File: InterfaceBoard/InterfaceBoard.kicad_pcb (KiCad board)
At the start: 2 copper layers, 100 x 86 mm, 167 parts, among them J1 SWD, J2 USB_B, J3 Keithley_50-Pin_Connector, J4 DB9_Female_MountingHoles, J5 SPI, J6 RS232, J7 UART, P1 RB1-125BAG1A, Q1 BC848W, Q2 BC848W, Q3 BC848W, U1 W5500, U2 FT231XQ, U3 MAX3232, U4 STM32G0B1RET, U5 AP62250Z6, Y1 25 MHz, Y2 32.768 kHz, Y3 24 MHz

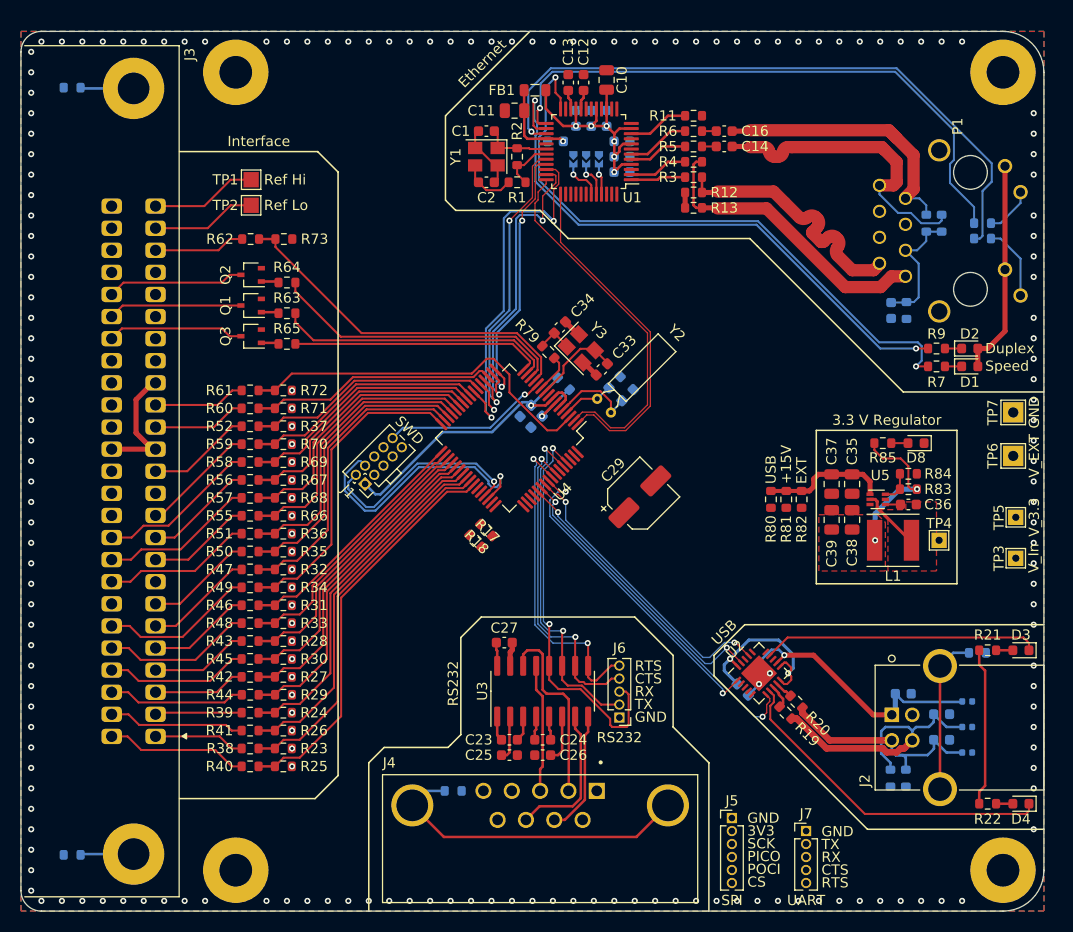
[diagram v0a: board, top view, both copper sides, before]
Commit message: InterfaceBoard: Place and route buttons and LEDs.
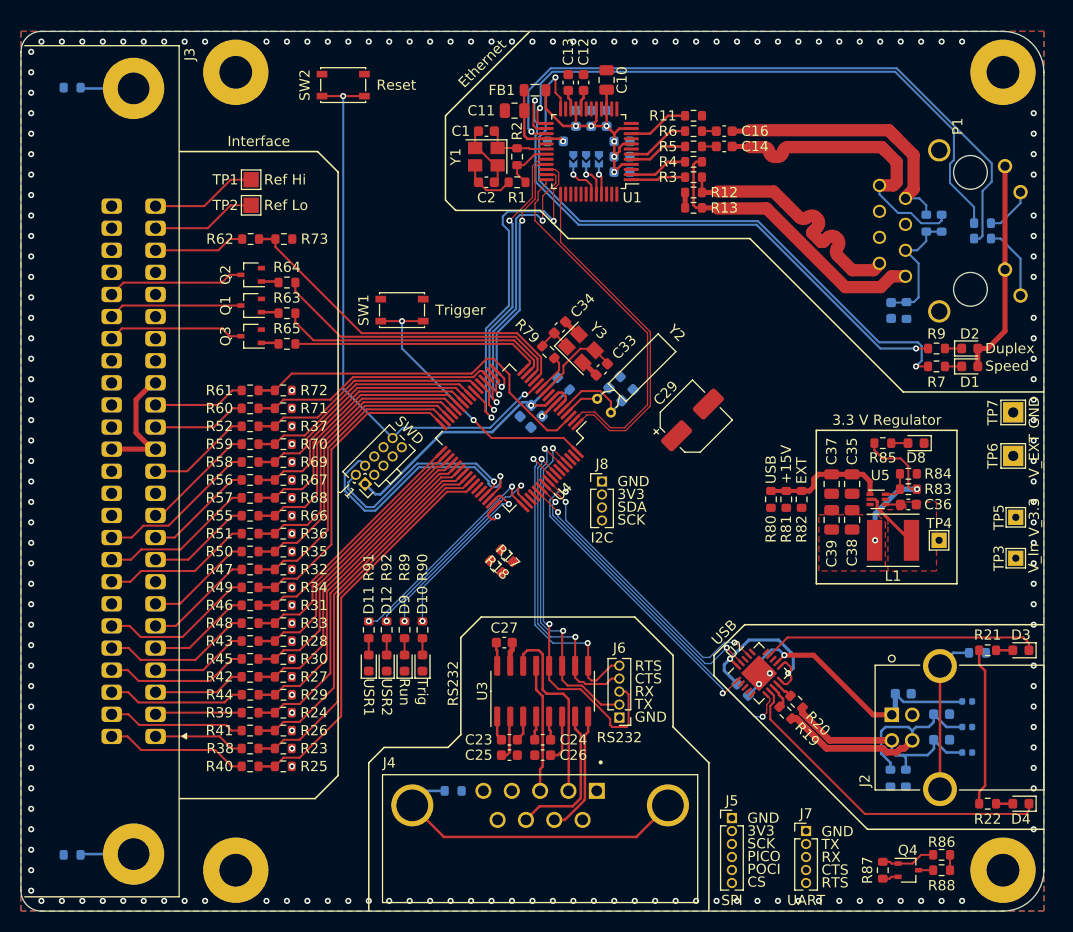
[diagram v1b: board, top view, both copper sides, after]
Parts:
- added D10: Red, LED_SMD:LED_0603_1608Metric, F.Cu at (79.2, 90.8)
- added D11: Red, LED_SMD:LED_0603_1608Metric, F.Cu at (74.0, 90.8)
- added D12: Red, LED_SMD:LED_0603_1608Metric, F.Cu at (75.7, 90.8)
- added D9: Red, LED_SMD:LED_0603_1608Metric, F.Cu at (77.5, 90.8)
- added J8: I2C, Connector_PinHeader_1.27mm:PinHeader_1x04_P1.27mm_Vertical, F.Cu at (96.8, 73.0)
- added Q4: BC856W, Package_TO_SOT_SMD:SOT-323_SC-70, F.Cu at (126.8, 111.0)
- added R86: 10k, Resistor_SMD:R_0603_1608Metric, F.Cu at (130.0, 109.5)
- added R87: 180k, Resistor_SMD:R_0603_1608Metric, F.Cu at (124.2, 111.0)
- added R88: 0, Resistor_SMD:R_0603_1608Metric, F.Cu at (130.0, 111.0)
- added R89: 1.8k, Resistor_SMD:R_0603_1608Metric, F.Cu at (77.5, 87.5)
- added R90: 1.8k, Resistor_SMD:R_0603_1608Metric, F.Cu at (79.2, 87.5)
- added R91: 1.8k, Resistor_SMD:R_0603_1608Metric, F.Cu at (74.0, 87.5)
- added R92: 1.8k, Resistor_SMD:R_0603_1608Metric, F.Cu at (75.7, 87.5)
- added SW1: PTS810, Button_Switch_SMD:SW_SPST_PTS810, F.Cu at (77.2, 56.2)
- added SW2: PTS810, Button_Switch_SMD:SW_SPST_PTS810, F.Cu at (71.5, 34.2)
- moved C29 9.11 mm to (105.6, 67.0)
- moved R17 3.20 mm to (87.5, 80.2)
- moved R18 3.20 mm to (86.4, 81.3)
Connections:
- R75 pad 2: /MCU/USB_PULLUP -> Net-(R75-Pad2)
- R76 pad 2: /MCU/USB_PULLUP -> Net-(R75-Pad2)
- U4 pad 47: unconnected-(U4-Pad47) -> /MCU/LED_RUN
- U4 pad 48: unconnected-(U4-Pad48) -> /MCU/LED_TRIG
- U4 pad 49: unconnected-(U4-Pad49) -> /MCU/LED_USR1
- U4 pad 50: unconnected-(U4-Pad50) -> /MCU/LED_USR2
- U4 pad 59: unconnected-(U4-Pad59) -> /MCU/USB_PULLUP
- U4 pad 64: unconnected-(U4-Pad64) -> /MCU/BTN_TRIG
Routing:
- net /MCU/NRST: track 16.4 -> 56.0 mm, vias 1 -> 2
- net /MCU/BTN_TRIG: track 0.00 -> 28.2 mm, vias 0 -> 2
- net /MCU/LED_USR1: track 0.00 -> 21.8 mm, vias 0 -> 2
- net /MCU/LED_USR2: track 0.00 -> 21.1 mm, vias 0 -> 2
- net /MCU/LED_RUN: track 0.00 -> 18.3 mm, vias 0 -> 2
- net /MCU/LED_TRIG: track 0.00 -> 15.9 mm, vias 0 -> 2
- net Net-(Q4-Pad1): track 0.00 -> 5.35 mm
- net Net-(D11-Pad2): track 0.00 -> 1.64 mm
- net Net-(D9-Pad2): track 0.00 -> 1.64 mm
- net Net-(D12-Pad2): track 0.00 -> 1.64 mm
- net Net-(D10-Pad2): track 0.00 -> 1.64 mm
- net +3V3: track 78.3 -> 79.9 mm
- net /MCU/USB_PULLUP: track 0.00 -> 1.50 mm
- net Net-(R75-Pad2): track 0.00 -> 1.43 mm
- net /Ethernet Interface/POCI: track 35.5 -> 36.2 mm
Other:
- board text added: "Reset"
- board text added: "Run"
- board text added: "SDA"
- board text added: "Trig"
- board text added: "Trigger"
- board text added: "USR1"
- board text added: "USR2"

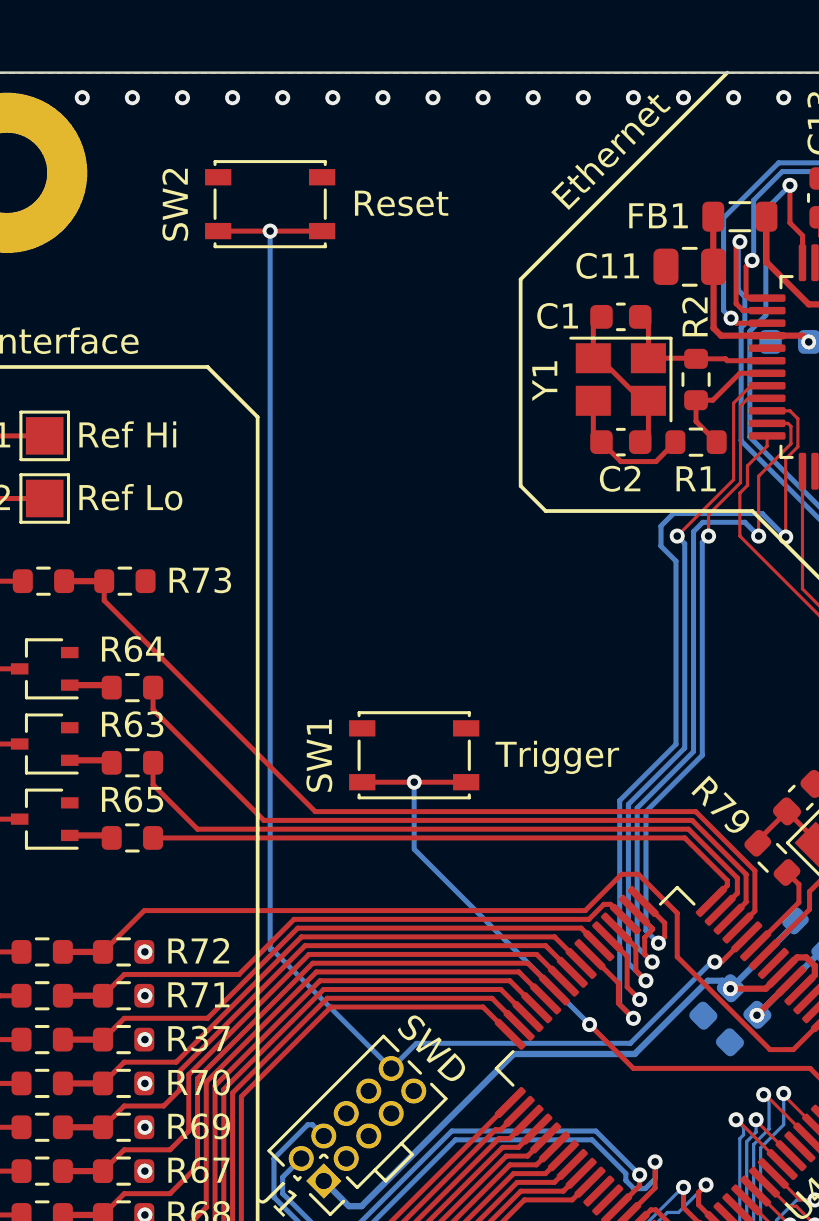
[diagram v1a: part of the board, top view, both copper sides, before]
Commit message: InterfaceBoard: Swap trigger and reset buttons
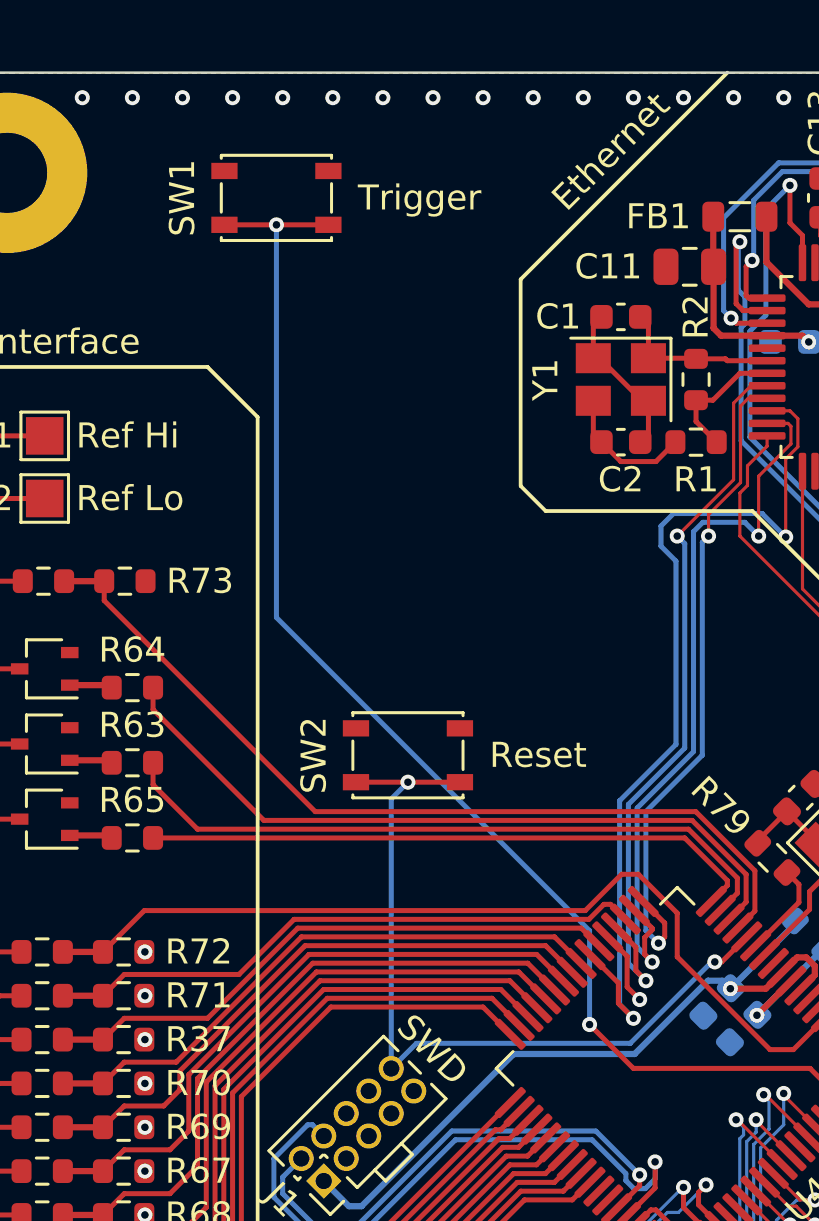
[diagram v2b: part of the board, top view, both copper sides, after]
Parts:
- moved SW1 22.9 mm to (71.8, 34.0)
- moved SW2 22.7 mm to (77.0, 56.2)
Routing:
- net /MCU/BTN_TRIG: track 28.2 -> 52.7 mm
- net /MCU/NRST: track 56.0 -> 32.2 mm
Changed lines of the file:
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@@
   )
   (footprint "Button_Switch_SMD:SW_SPST_PTS810" (layer "F.Cu")
-    (at 71.5 34.25)
+    (at 77 56.25)
     (descr "C&K Components, PTS 810 Series, Microminiature SMT Top Actuated, http://www.ckswitches.com/media/1476/pts810.pdf")
     (tags "SPST Button Switch")
@@
   )
   (footprint "Button_Switch_SMD:SW_SPST_PTS810" (layer "F.Cu")
-    (at 77.25 56.25)
+    (at 71.75 34)
     (descr "C&K Components, PTS 810 Series, Microminiature SMT Top Actuated, http://www.ckswitches.com/media/1476/pts810.pdf")
     (tags "SPST Button Switch")
@@
     (effects (font (size 1 1) (thickness 0.15)) (justify left))
   )
-  (gr_text "Trigger" (at 80.499999 56.25) (layer "F.SilkS")
+  (gr_text "Trigger" (at 74.999999 34) (layer "F.SilkS")
     (effects (font (size 1 1) (thickness 0.15)) (justify left))
   )
@@
     (effects (font (size 1 1) (thickness 0.15)) (justify left))
   )
-  (gr_text "Reset" (at 74.750001 34.249998) (layer "F.SilkS")
+  (gr_text "Reset" (at 80.250001 56.249998) (layer "F.SilkS")
     (effects (font (size 1 1) (thickness 0.15)) (justify left))
   )
@@
   (segment (start 89.525126 64.5) (end 90.525394 63.499732) (width 0.2) (layer "F.Cu") (net 16))
   (segment (start 89.25 64.5) (end 89.525126 64.5) (width 0.2) (layer "F.Cu") (net 16))
-  (segment (start 71.5 35.324999) (end 69.425 35.324999) (width 0.2) (layer "F.Cu") (net 16))
-  (segment (start 73.575 35.324999) (end 71.5 35.324999) (width 0.2) (layer "F.Cu") (net 16))
+  (segment (start 77 57.324999) (end 74.925 57.324999) (width 0.2) (layer "F.Cu") (net 16))
+  (segment (start 79.075 57.324999) (end 77 57.324999) (width 0.2) (layer "F.Cu") (net 16))
   (via (at 89.25 64.5) (size 0.6) (drill 0.3) (layers "F.Cu" "B.Cu") (free) (net 16))
-  (via (at 71.5 35.324999) (size 0.6) (drill 0.3) (layers "F.Cu" "B.Cu") (net 16))
+  (via (at 77 57.324999) (size 0.6) (drill 0.3) (layers "F.Cu" "B.Cu") (net 16))
   (segment (start 77.337833 67.75) (end 76.332897 68.754936) (width 0.2) (layer "B.Cu") (net 16))
-  (segment (start 71.577961 64) (end 76.332897 68.754936) (width 0.2) (layer "B.Cu") (net 16))
   (segment (start 85.875 67.75) (end 77.337833 67.75) (width 0.2) (layer "B.Cu") (net 16))
   (segment (start 89.25 64.5) (end 89.125 64.5) (width 0.2) (layer "B.Cu") (net 16))
+  (segment (start 76.332897 57.992102) (end 76.332897 68.754936) (width 0.2) (layer "B.Cu") (net 16))
   (segment (start 89.125 64.5) (end 85.875 67.75) (width 0.2) (layer "B.Cu") (net 16))
-  (segment (start 71.5 64) (end 71.577961 64) (width 0.2) (layer "B.Cu") (net 16))
-  (segment (start 71.5 35.324999) (end 71.5 64) (width 0.2) (layer "B.Cu") (net 16))
+  (segment (start 77 57.324999) (end 76.332897 57.992102) (width 0.2) (layer "B.Cu") (net 16))
   (segment (start 88.5 42.925) (end 89.325 43.75) (width 0.2) (layer "F.Cu") (net 20))
   (segment (start 89.175 42.075) (end 90.25 41) (width 0.2) (layer "F.Cu") (net 20))
@@
   (segment (start 87.8 74.5) (end 88.9 73.4) (width 0.127) (layer "B.Cu") (net 200))
   (segment (start 94.414481 70.111181) (end 93.0533 68.75) (width 0.2) (layer "F.Cu") (net 201))
-  (segment (start 77.25 57.325) (end 75.175 57.325) (width 0.2) (layer "F.Cu") (net 201))
+  (segment (start 71.75 35.075) (end 69.675 35.075) (width 0.2) (layer "F.Cu") (net 201))
   (segment (start 86 68.75) (end 84.25 67) (width 0.2) (layer "F.Cu") (net 201))
-  (segment (start 79.325001 57.325001) (end 77.25 57.325) (width 0.2) (layer "F.Cu") (net 201))
+  (segment (start 73.825001 35.075001) (end 71.75 35.075) (width 0.2) (layer "F.Cu") (net 201))
   (segment (start 93.0533 68.75) (end 86 68.75) (width 0.2) (layer "F.Cu") (net 201))
-  (via (at 77.25 57.325) (size 0.6) (drill 0.3) (layers "F.Cu" "B.Cu") (net 201))
+  (via (at 71.75 35.075) (size 0.6) (drill 0.3) (layers "F.Cu" "B.Cu") (net 201))
   (via (at 84.25 67) (size 0.6) (drill 0.3) (layers "F.Cu" "B.Cu") (net 201))
-  (segment (start 77.25 60) (end 77.25 57.325) (width 0.2) (layer "B.Cu") (net 201))
-  (segment (start 84.25 67) (end 77.25 60) (width 0.2) (layer "B.Cu") (net 201))
+  (segment (start 71.75 50.75) (end 84.25 63.25) (width 0.2) (layer "B.Cu") (net 201))
+  (segment (start 71.75 35.075) (end 71.75 50.75) (width 0.2) (layer "B.Cu") (net 201))
+  (segment (start 84.25 63.25) (end 84.25 67) (width 0.2) (layer "B.Cu") (net 201))
   (zone (net 4) (net_name "+3V3") (layer "F.Cu") (hatch edge 0.508)
     (priority 1)

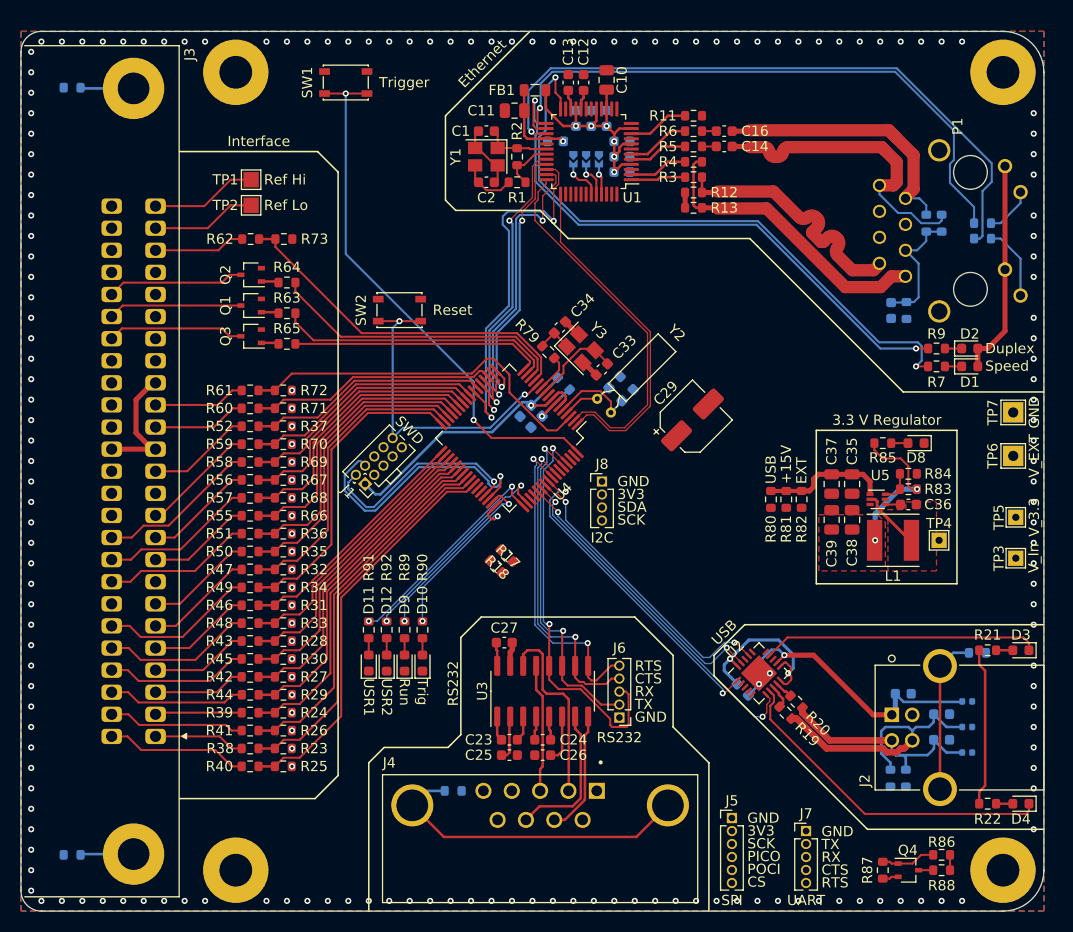
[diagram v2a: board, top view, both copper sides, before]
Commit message: InterfaceBoard: Route MCU USB
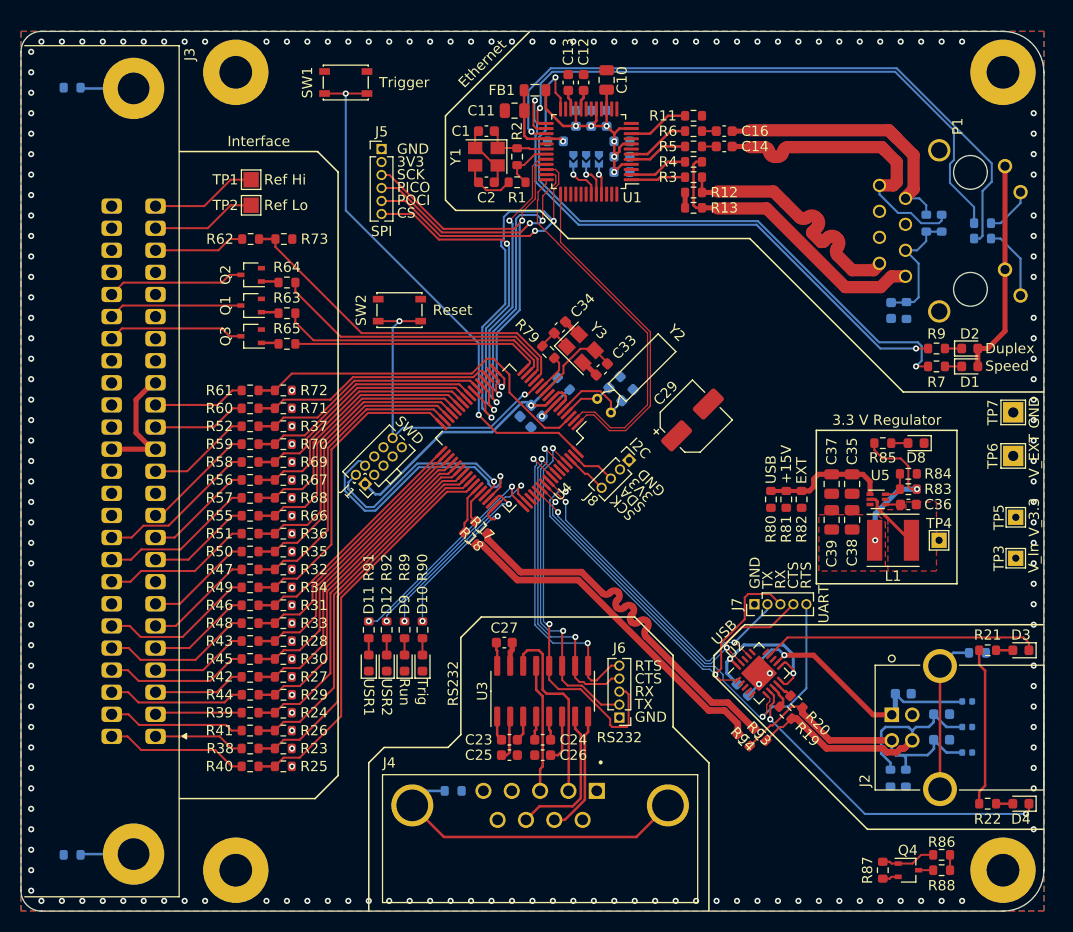
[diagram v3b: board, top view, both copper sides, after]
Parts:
- added R93: 0, Resistor_SMD:R_0603_1608Metric, F.Cu at (112.2, 97.8)
- added R94: 0, Resistor_SMD:R_0603_1608Metric, F.Cu at (110.7, 98.3)
- R17, R18, R19, R20: value 27R -> 27
- moved J5 73.8 mm to (75.2, 40.5)
- moved J7 22.7 mm to (111.7, 85.0), turned to 90 degrees
- moved R17 3.72 mm to (85.0, 77.5)
- moved R18 3.72 mm to (83.9, 78.6)
- moved J8 3.37 mm to (99.5, 70.9), turned to -45 degrees
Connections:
- R17 pad 1: /USB/USBB_D+ -> /USB/MCU_USBB_D+
- R18 pad 1: /USB/USBB_D- -> /USB/MCU_USBB_D-
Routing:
- net /USB/MCU_USBB_D+: track 0.00 -> 38.3 mm
- net /USB/MCU_USBB_D-: track 0.00 -> 33.8 mm
- net /MCU/SPI_CS_USR: track 3.03 -> 34.1 mm, vias 1 -> 2
- net /Ethernet Interface/POCI: track 36.2 -> 55.1 mm, vias 2 -> 3
- net /Ethernet Interface/PICO: track 29.9 -> 47.9 mm, vias 2 -> 3
- net /Ethernet Interface/SCK: track 26.5 -> 42.8 mm
- net /MCU/USB_UART_RTS: track 34.6 -> 48.6 mm
- net /MCU/USB_UART_RX: track 31.9 -> 43.3 mm
- net /MCU/USB_UART_CTS: track 28.4 -> 37.0 mm
- net /USB/USBB_D-: track 22.4 -> 29.2 mm
- net /MCU/USB_UART_TX: track 29.1 -> 34.6 mm
- net /MCU/USB_D-: track 0.00 -> 4.85 mm
- net /MCU/I2C_SDA: track 0.00 -> 4.53 mm
- net /MCU/I2C_SCK: track 0.00 -> 4.21 mm
- net /MCU/USB_D+: track 0.00 -> 3.49 mm
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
